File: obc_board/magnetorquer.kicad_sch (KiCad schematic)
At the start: 48 parts, among them U21 STSPIN240, U22 STSPIN240, U23 AP22652A

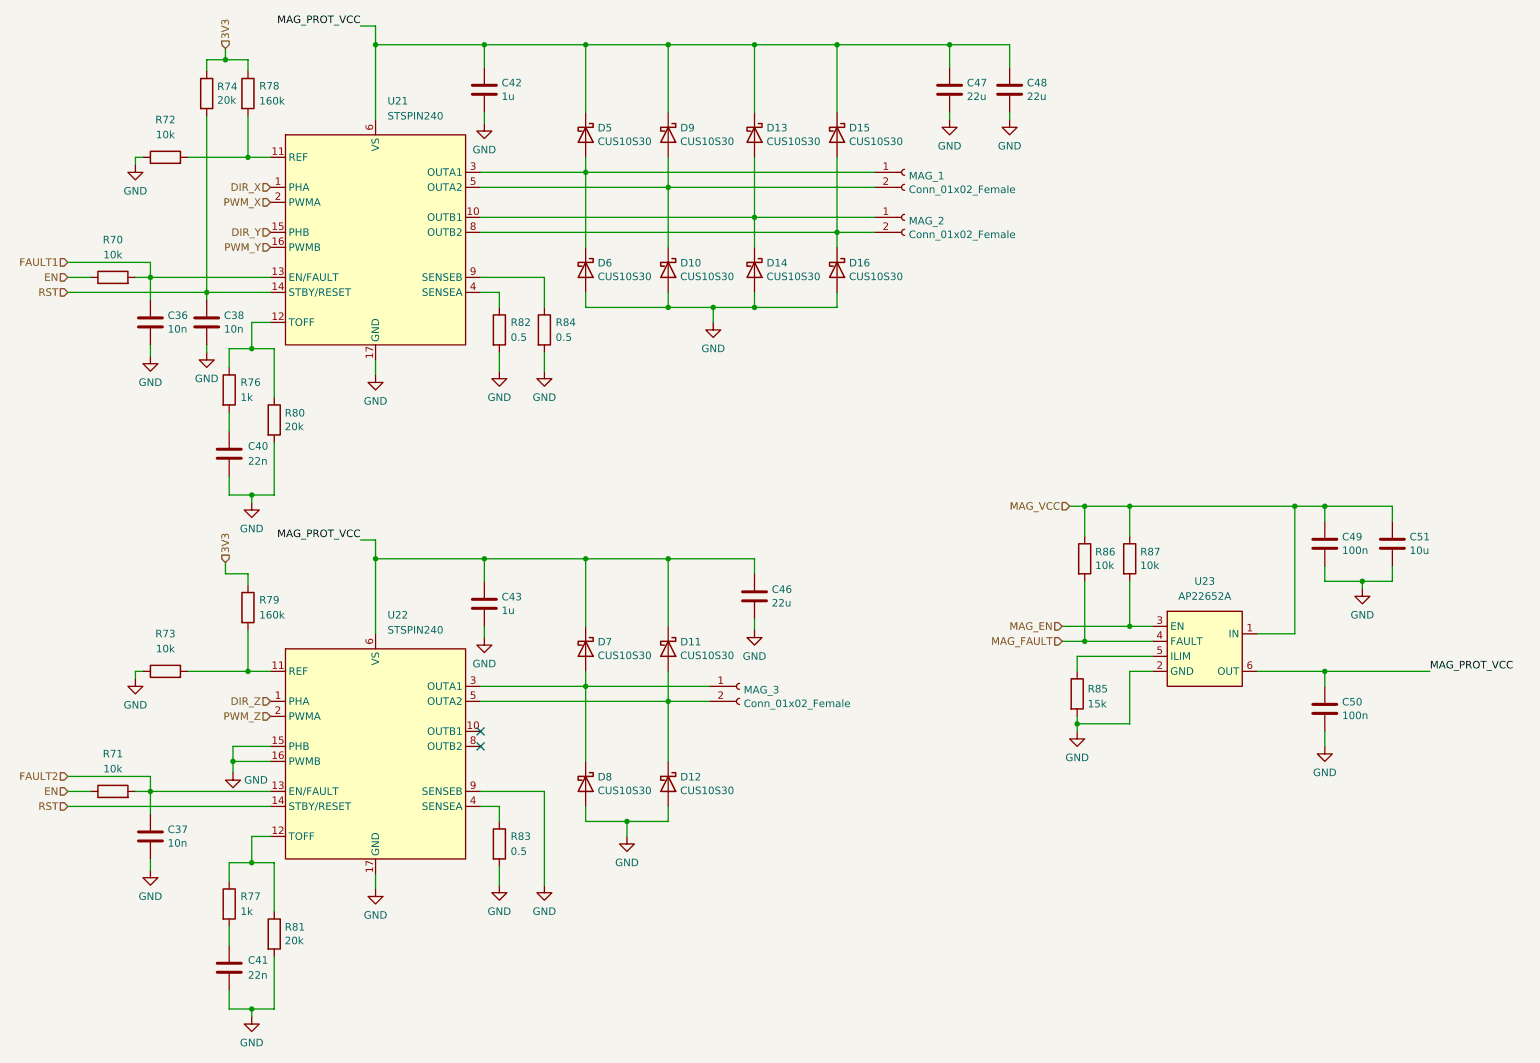
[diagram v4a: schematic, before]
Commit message: changed picoblade symbols to include mounting pins, added photodiode circuitry and additional testpoints, added GPS to FTDI jumper
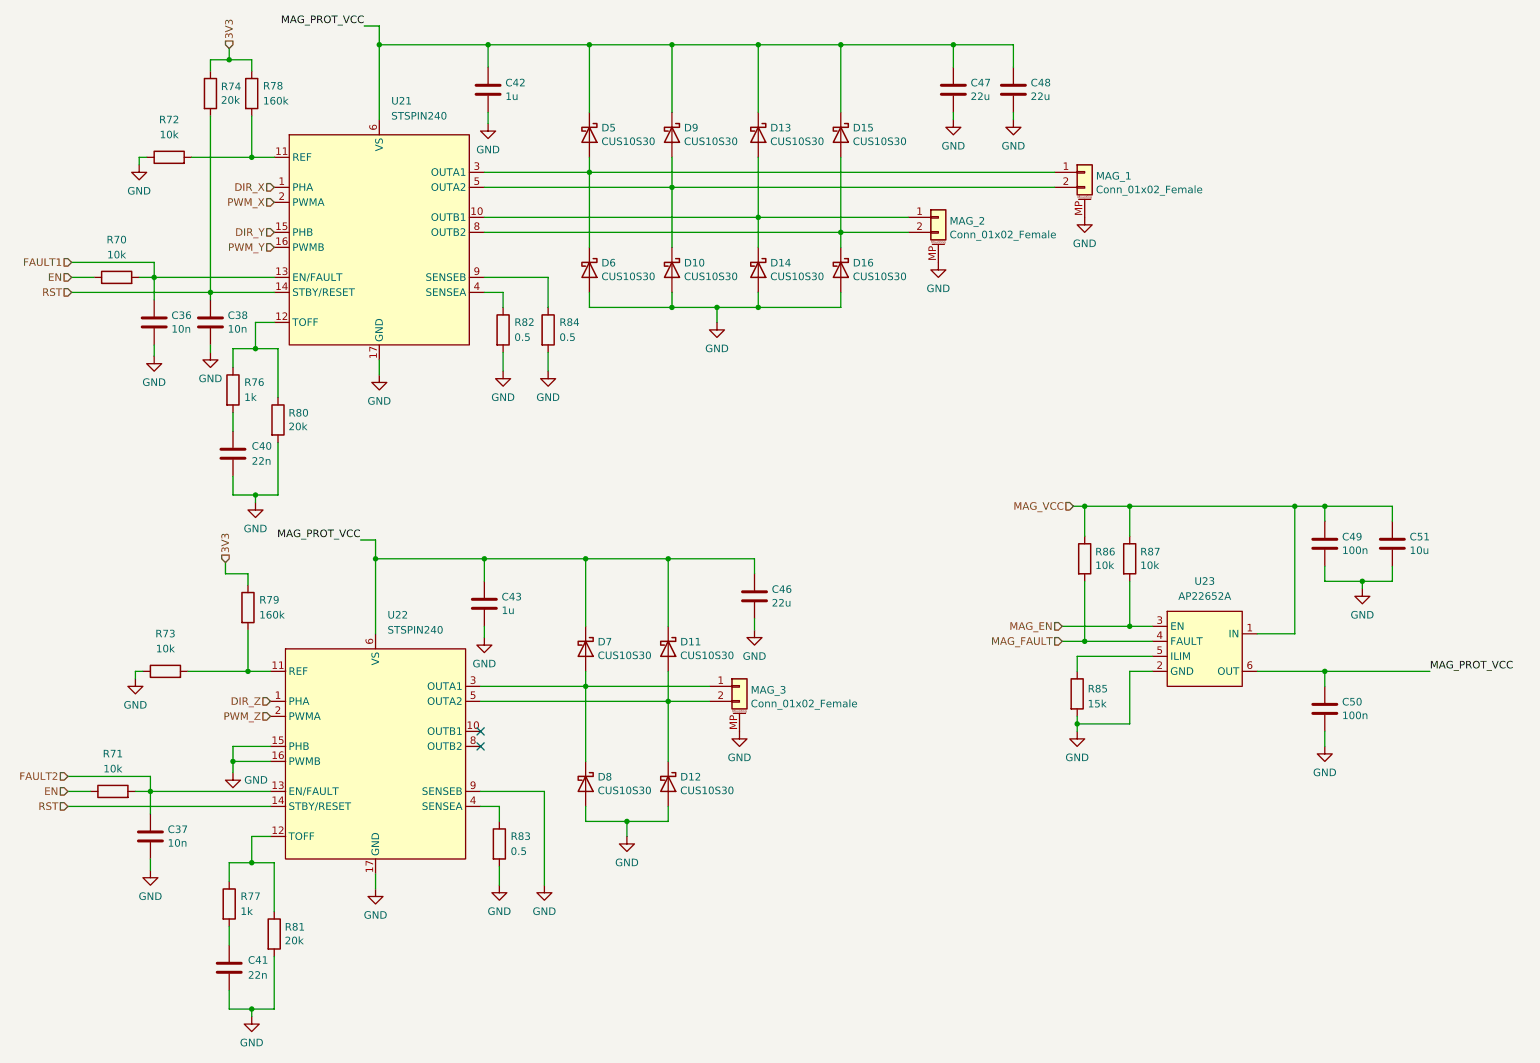
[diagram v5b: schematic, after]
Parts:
- MAG_1, MAG_2, MAG_3: symbol Connector:Conn_01x02_Female -> Connector_Generic_MountingPin:Conn_01x02_MountingPin
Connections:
- net GND: now also MAG_1.MP (MountPin), MAG_2.MP (MountPin), MAG_3.MP (MountPin)
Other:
- moved on the sheet: C36, C38, C40, C42, C47, C48, D10, D13, D14, D15, D16, D5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
